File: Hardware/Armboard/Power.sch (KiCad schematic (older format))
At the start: 7 parts

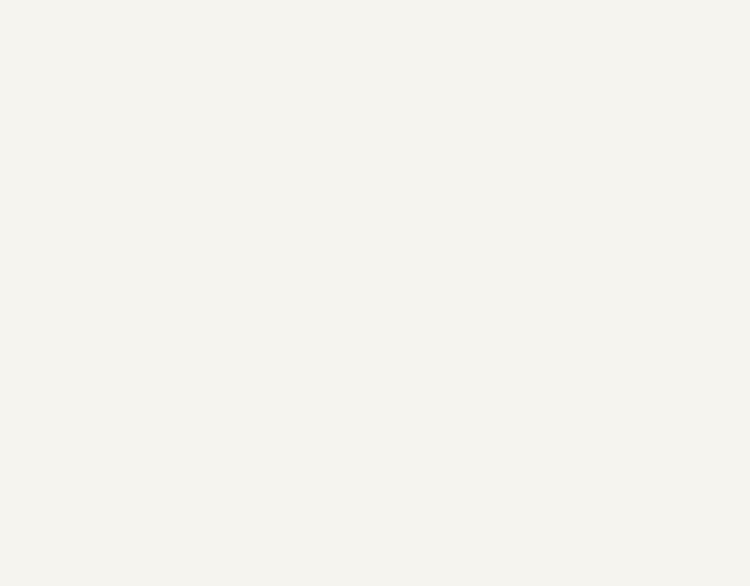
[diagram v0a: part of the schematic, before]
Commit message: Added Anderson connectors to power section
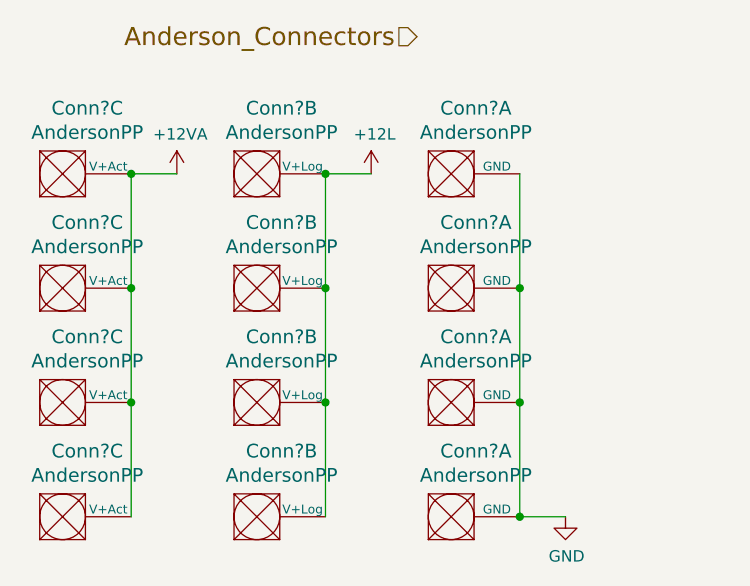
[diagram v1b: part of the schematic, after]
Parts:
- added Conn? (x12): AndersonPP, symbol MRDT_Connectors:AndersonPP
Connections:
- net +12VA: now also Conn?.3 (V+Act), Conn?.3 (V+Act), Conn?.3 (V+Act), Conn?.3 (V+Act)
- net GND: now also Conn?.1 (GND), Conn?.1 (GND), Conn?.1 (GND), Conn?.1 (GND)
- new net +12L: Conn?.2 (V+Log), Conn?.2 (V+Log), Conn?.2 (V+Log), Conn?.2 (V+Log)
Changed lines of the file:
@@
 Text HLabel 9650 1400 0    79   Input ~ 0
 Capacitor_Train
+$Comp
+L MRDT_Connectors:AndersonPP Conn?
+U 3 1 5F67B2AF
+P 2100 2000
+F 0 "Conn?" H 2308 2387 60  0000 C CNN
+F 1 "AndersonPP" H 2308 2281 60  0000 C CNN
+F 2 "" H 1950 1450 60  0001 C CNN
+F 3 "" H 1950 1450 60  0001 C CNN
+	3    2100 2000
+	1    0    0    -1
+$EndComp
+$Comp
+L MRDT_Connectors:AndersonPP Conn?
+U 2 1 5F67B746
+P 2950 2000
+F 0 "Conn?" H 3158 2387 60  0000 C CNN
+F 1 "AndersonPP" H 3158 2281 60  0000 C CNN
+F 2 "" H 2800 1450 60  0001 C CNN
+F 3 "" H 2800 1450 60  0001 C CNN
+	2    2950 2000
+	1    0    0    -1
+$EndComp
+$Comp
+L MRDT_Connectors:AndersonPP Conn?
+U 1 1 5F67BE24
+P 3800 2000
+F 0 "Conn?" H 4008 2387 60  0000 C CNN
+F 1 "AndersonPP" H 4008 2281 60  0000 C CNN
+F 2 "" H 3650 1450 60  0001 C CNN
+F 3 "" H 3650 1450 60  0001 C CNN
+	1    3800 2000
+	1    0    0    -1
+$EndComp
+$Comp
+L MRDT_Connectors:AndersonPP Conn?
+U 3 1 5F67E65A
+P 2100 2500
+F 0 "Conn?" H 2308 2887 60  0000 C CNN
+F 1 "AndersonPP" H 2308 2781 60  0000 C CNN
+F 2 "" H 1950 1950 60  0001 C CNN
+F 3 "" H 1950 1950 60  0001 C CNN
+	3    2100 2500
+	1    0    0    -1
+$EndComp
+$Comp
+L MRDT_Connectors:AndersonPP Conn?
+U 2 1 5F67E660
+P 2950 2500
+F 0 "Conn?" H 3158 2887 60  0000 C CNN
+F 1 "AndersonPP" H 3158 2781 60  0000 C CNN
+F 2 "" H 2800 1950 60  0001 C CNN
+F 3 "" H 2800 1950 60  0001 C CNN
+	2    2950 2500
+	1    0    0    -1
+$EndComp
+$Comp
+L MRDT_Connectors:AndersonPP Conn?
+U 1 1 5F67E666
+P 3800 2500
+F 0 "Conn?" H 4008 2887 60  0000 C CNN
+F 1 "AndersonPP" H 4008 2781 60  0000 C CNN
+F 2 "" H 3650 1950 60  0001 C CNN
+F 3 "" H 3650 1950 60  0001 C CNN
+	1    3800 2500
+	1    0    0    -1
+$EndComp
+$Comp
+L MRDT_Connectors:AndersonPP Conn?
+U 3 1 5F67F13B
+P 2100 3000
+F 0 "Conn?" H 2308 3387 60  0000 C CNN
+F 1 "AndersonPP" H 2308 3281 60  0000 C CNN
+F 2 "" H 1950 2450 60  0001 C CNN
+F 3 "" H 1950 2450 60  0001 C CNN
+	3    2100 3000
+	1    0    0    -1
+$EndComp
+$Comp
+L MRDT_Connectors:AndersonPP Conn?
+U 2 1 5F67F141
+P 2950 3000
+F 0 "Conn?" H 3158 3387 60  0000 C CNN
+F 1 "AndersonPP" H 3158 3281 60  0000 C CNN
+F 2 "" H 2800 2450 60  0001 C CNN
+F 3 "" H 2800 2450 60  0001 C CNN
+	2    2950 3000
+	1    0    0    -1
+$EndComp
+$Comp
+L MRDT_Connectors:AndersonPP Conn?
+U 1 1 5F67F147
+P 3800 3000
+F 0 "Conn?" H 4008 3387 60  0000 C CNN
+F 1 "AndersonPP" H 4008 3281 60  0000 C CNN
+F 2 "" H 3650 2450 60  0001 C CNN
+F 3 "" H 3650 2450 60  0001 C CNN
+	1    3800 3000
+	1    0    0    -1
+$EndComp
+$Comp
+L MRDT_Connectors:AndersonPP Conn?
+U 3 1 5F67F9E7
+P 2100 3500
+F 0 "Conn?" H 2308 3887 60  0000 C CNN
+F 1 "AndersonPP" H 2308 3781 60  0000 C CNN
+F 2 "" H 1950 2950 60  0001 C CNN
+F 3 "" H 1950 2950 60  0001 C CNN
+	3    2100 3500
+	1    0    0    -1
+$EndComp
+$Comp
+L MRDT_Connectors:AndersonPP Conn?
+U 2 1 5F67F9ED
+P 2950 3500
+F 0 "Conn?" H 3158 3887 60  0000 C CNN
+F 1 "AndersonPP" H 3158 3781 60  0000 C CNN
+F 2 "" H 2800 2950 60  0001 C CNN
+F 3 "" H 2800 2950 60  0001 C CNN
+	2    2950 3500
+	1    0    0    -1
+$EndComp
+$Comp
+L MRDT_Connectors:AndersonPP Conn?
+U 1 1 5F67F9F3
+P 3800 3500
+F 0 "Conn?" H 4008 3887 60  0000 C CNN
+F 1 "AndersonPP" H 4008 3781 60  0000 C CNN
+F 2 "" H 3650 2950 60  0001 C CNN
+F 3 "" H 3650 2950 60  0001 C CNN
+	1    3800 3500
+	1    0    0    -1
+$EndComp
+Wire Wire Line
+	2500 3400 2500 2900
+Connection ~ 2500 2400
+Wire Wire Line
+	2500 2400 2500 1900
+Connection ~ 2500 2900
+Wire Wire Line
+	2500 2900 2500 2400
+Wire Wire Line
+	3350 1900 3350 2400
+Connection ~ 3350 2400
+Wire Wire Line
+	3350 2400 3350 2900
+Connection ~ 3350 2900
+Wire Wire Line
+	3350 2900 3350 3400
+Wire Wire Line
+	4200 1900 4200 2400
+Connection ~ 4200 2400
+Wire Wire Line
+	4200 2400 4200 2900
+Connection ~ 4200 2900
+Wire Wire Line
+	4200 2900 4200 3400
+$Comp
+L power:+12VA #PWR?
+U 1 1 5F680A3E
+P 2700 1900
+F 0 "#PWR?" H 2700 1750 50  0001 C CNN
+F 1 "+12VA" H 2715 2073 50  0000 C CNN
+F 2 "" H 2700 1900 50  0001 C CNN
+F 3 "" H 2700 1900 50  0001 C CNN
+	1    2700 1900
+	1    0    0    -1
+$EndComp
+$Comp
+L power:+12L #PWR?
+U 1 1 5F6813B5
+P 3550 1900
+F 0 "#PWR?" H 3550 1750 50  0001 C CNN
+F 1 "+12L" H 3565 2073 50  0000 C CNN
+F 2 "" H 3550 1900 50  0001 C CNN
+F 3 "" H 3550 1900 50  0001 C CNN
+	1    3550 1900
+	1    0    0    -1
+$EndComp
+$Comp
+L power:GND #PWR?
+U 1 1 5F68170C
+P 4400 3400
+F 0 "#PWR?" H 4400 3150 50  0001 C CNN
+F 1 "GND" H 4405 3227 50  0000 C CNN
+F 2 "" H 4400 3400 50  0001 C CNN
+F 3 "" H 4400 3400 50  0001 C CNN
+	1    4400 3400
+	1    0    0    -1
+$EndComp
+Wire Wire Line
+	2500 1900 2700 1900
+Connection ~ 2500 1900
+Wire Wire Line
+	3350 1900 3550 1900
+Connection ~ 3350 1900
+Wire Wire Line
+	4200 3400 4400 3400
+Connection ~ 4200 3400
+Text HLabel 3750 1300 0    79   Input ~ 0
+Anderson_Connectors
 $EndSCHEMATC

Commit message: Power Board Schematic Update
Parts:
- added 10uF: C6, symbol Device:C
- added 10uF: C7, symbol Device:C
- Conn? (x12): symbol MRDT_Connectors:AndersonPP -> Armboard-rescue:AndersonPP-MRDT_Connectors
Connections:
- net +12L: now also 10uF.1
- net GND: now also 10uF.2, 10uF.2
- new net +3V3: 10uF.1
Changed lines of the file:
@@
 Capacitor_Train
 $Comp
-L MRDT_Connectors:AndersonPP Conn?
+L Armboard-rescue:AndersonPP-MRDT_Connectors Conn?
 U 3 1 5F67B2AF
 P 2100 2000
+AR Path="/5F67B2AF" Ref="Conn?"  Part="3"
+AR Path="/5F67ABAC/5F67B2AF" Ref="Conn?"  Part="3"
 F 0 "Conn?" H 2308 2387 60  0000 C CNN
 F 1 "AndersonPP" H 2308 2281 60  0000 C CNN
@@
 $EndComp
 $Comp
-L MRDT_Connectors:AndersonPP Conn?
+L Armboard-rescue:AndersonPP-MRDT_Connectors Conn?
 U 2 1 5F67B746
 P 2950 2000
+AR Path="/5F67B746" Ref="Conn?"  Part="2"
+AR Path="/5F67ABAC/5F67B746" Ref="Conn?"  Part="2"
 F 0 "Conn?" H 3158 2387 60  0000 C CNN
 F 1 "AndersonPP" H 3158 2281 60  0000 C CNN
@@
 $EndComp
 $Comp
-L MRDT_Connectors:AndersonPP Conn?
+L Armboard-rescue:AndersonPP-MRDT_Connectors Conn?
 U 1 1 5F67BE24
 P 3800 2000
+AR Path="/5F67BE24" Ref="Conn?"  Part="1"
+AR Path="/5F67ABAC/5F67BE24" Ref="Conn?"  Part="1"
 F 0 "Conn?" H 4008 2387 60  0000 C CNN
 F 1 "AndersonPP" H 4008 2281 60  0000 C CNN
@@
 $EndComp
 $Comp
-L MRDT_Connectors:AndersonPP Conn?
+L Armboard-rescue:AndersonPP-MRDT_Connectors Conn?
 U 3 1 5F67E65A
 P 2100 2500
+AR Path="/5F67E65A" Ref="Conn?"  Part="3"
+AR Path="/5F67ABAC/5F67E65A" Ref="Conn?"  Part="3"
 F 0 "Conn?" H 2308 2887 60  0000 C CNN
 F 1 "AndersonPP" H 2308 2781 60  0000 C CNN
@@
 $EndComp
 $Comp
-L MRDT_Connectors:AndersonPP Conn?
+L Armboard-rescue:AndersonPP-MRDT_Connectors Conn?
 U 2 1 5F67E660
 P 2950 2500
+AR Path="/5F67E660" Ref="Conn?"  Part="2"
+AR Path="/5F67ABAC/5F67E660" Ref="Conn?"  Part="2"
 F 0 "Conn?" H 3158 2887 60  0000 C CNN
 F 1 "AndersonPP" H 3158 2781 60  0000 C CNN
@@
 $EndComp
 $Comp
-L MRDT_Connectors:AndersonPP Conn?
+L Armboard-rescue:AndersonPP-MRDT_Connectors Conn?
 U 1 1 5F67E666
 P 3800 2500
+AR Path="/5F67E666" Ref="Conn?"  Part="1"
+AR Path="/5F67ABAC/5F67E666" Ref="Conn?"  Part="1"
 F 0 "Conn?" H 4008 2887 60  0000 C CNN
 F 1 "AndersonPP" H 4008 2781 60  0000 C CNN
@@
 $EndComp
 $Comp
-L MRDT_Connectors:AndersonPP Conn?
+L Armboard-rescue:AndersonPP-MRDT_Connectors Conn?
 U 3 1 5F67F13B
 P 2100 3000
+AR Path="/5F67F13B" Ref="Conn?"  Part="3"
+AR Path="/5F67ABAC/5F67F13B" Ref="Conn?"  Part="3"
 F 0 "Conn?" H 2308 3387 60  0000 C CNN
 F 1 "AndersonPP" H 2308 3281 60  0000 C CNN
@@
 $EndComp
 $Comp
-L MRDT_Connectors:AndersonPP Conn?
+L Armboard-rescue:AndersonPP-MRDT_Connectors Conn?
 U 2 1 5F67F141
 P 2950 3000
+AR Path="/5F67F141" Ref="Conn?"  Part="2"
+AR Path="/5F67ABAC/5F67F141" Ref="Conn?"  Part="2"
 F 0 "Conn?" H 3158 3387 60  0000 C CNN
 F 1 "AndersonPP" H 3158 3281 60  0000 C CNN
@@
 $EndComp
 $Comp
-L MRDT_Connectors:AndersonPP Conn?
+L Armboard-rescue:AndersonPP-MRDT_Connectors Conn?
 U 1 1 5F67F147
 P 3800 3000
+AR Path="/5F67F147" Ref="Conn?"  Part="1"
+AR Path="/5F67ABAC/5F67F147" Ref="Conn?"  Part="1"
 F 0 "Conn?" H 4008 3387 60  0000 C CNN
 F 1 "AndersonPP" H 4008 3281 60  0000 C CNN
@@
 $EndComp
 $Comp
-L MRDT_Connectors:AndersonPP Conn?
+L Armboard-rescue:AndersonPP-MRDT_Connectors Conn?
 U 3 1 5F67F9E7
 P 2100 3500
+AR Path="/5F67F9E7" Ref="Conn?"  Part="3"
+AR Path="/5F67ABAC/5F67F9E7" Ref="Conn?"  Part="3"
 F 0 "Conn?" H 2308 3887 60  0000 C CNN
 F 1 "AndersonPP" H 2308 3781 60  0000 C CNN
@@
 $EndComp
 $Comp
-L MRDT_Connectors:AndersonPP Conn?
+L Armboard-rescue:AndersonPP-MRDT_Connectors Conn?
 U 2 1 5F67F9ED
 P 2950 3500
+AR Path="/5F67F9ED" Ref="Conn?"  Part="2"
+AR Path="/5F67ABAC/5F67F9ED" Ref="Conn?"  Part="2"
 F 0 "Conn?" H 3158 3887 60  0000 C CNN
 F 1 "AndersonPP" H 3158 3781 60  0000 C CNN
@@
 $EndComp
 $Comp
-L MRDT_Connectors:AndersonPP Conn?
+L Armboard-rescue:AndersonPP-MRDT_Connectors Conn?
 U 1 1 5F67F9F3
 P 3800 3500
+AR Path="/5F67F9F3" Ref="Conn?"  Part="1"
+AR Path="/5F67ABAC/5F67F9F3" Ref="Conn?"  Part="1"
 F 0 "Conn?" H 4008 3887 60  0000 C CNN
 F 1 "AndersonPP" H 4008 3781 60  0000 C CNN
@@
 Text HLabel 3750 1300 0    79   Input ~ 0
 Anderson_Connectors
+$Comp
+L power:+12L #PWR?
+U 1 1 5F67B836
+P 8500 2750
+F 0 "#PWR?" H 8500 2600 50  0001 C CNN
+F 1 "+12L" H 8515 2923 50  0000 C CNN
+F 2 "" H 8500 2750 50  0001 C CNN
+F 3 "" H 8500 2750 50  0001 C CNN
+	1    8500 2750
+	1    0    0    -1
+$EndComp
+$Comp
+L power:+3.3V #PWR?
+U 1 1 5F67BC4F
+P 10000 2700
+F 0 "#PWR?" H 10000 2550 50  0001 C CNN
+F 1 "+3.3V" H 10015 2873 50  0000 C CNN
+F 2 "" H 10000 2700 50  0001 C CNN
+F 3 "" H 10000 2700 50  0001 C CNN
+	1    10000 2700
+	1    0    0    -1
+$EndComp
+$Comp
+L Device:C 10uF
+U 1 1 5F67C9C2
+P 8500 3200
+F 0 "10uF" H 8615 3246 50  0000 L CNN
+F 1 "C6" H 8615 3155 50  0000 L CNN
+F 2 "" H 8538 3050 50  0001 C CNN
+F 3 "~" H 8500 3200 50  0001 C CNN
+	1    8500 3200
+	1    0    0    -1
+$EndComp
+$Comp
+L Device:C 10uF
+U 1 1 5F67D17F
+P 10000 3200
+F 0 "10uF" H 10115 3246 50  0000 L CNN
+F 1 "C7" H 10115 3155 50  0000 L CNN
+F 2 "" H 10038 3050 50  0001 C CNN
+F 3 "~" H 10000 3200 50  0001 C CNN
+	1    10000 3200
+	1    0    0    -1
+$EndComp
+Wire Wire Line
+	8500 2750 8500 3050
+Wire Wire Line
+	8500 3350 10000 3350
+Wire Wire Line
+	10000 3350 10250 3350
+Wire Wire Line
+	10250 3350 10250 3500
+Connection ~ 10000 3350
+Wire Wire Line
+	10000 2700 10000 3050
+$Comp
+L power:GND #PWR?
+U 1 1 5F6806AC
+P 10250 3500
+F 0 "#PWR?" H 10250 3250 50  0001 C CNN
+F 1 "GND" H 10255 3327 50  0000 C CNN
+F 2 "" H 10250 3500 50  0001 C CNN
+F 3 "" H 10250 3500 50  0001 C CNN
+	1    10250 3500
+	1    0    0    -1
+$EndComp
 $EndSCHEMATC

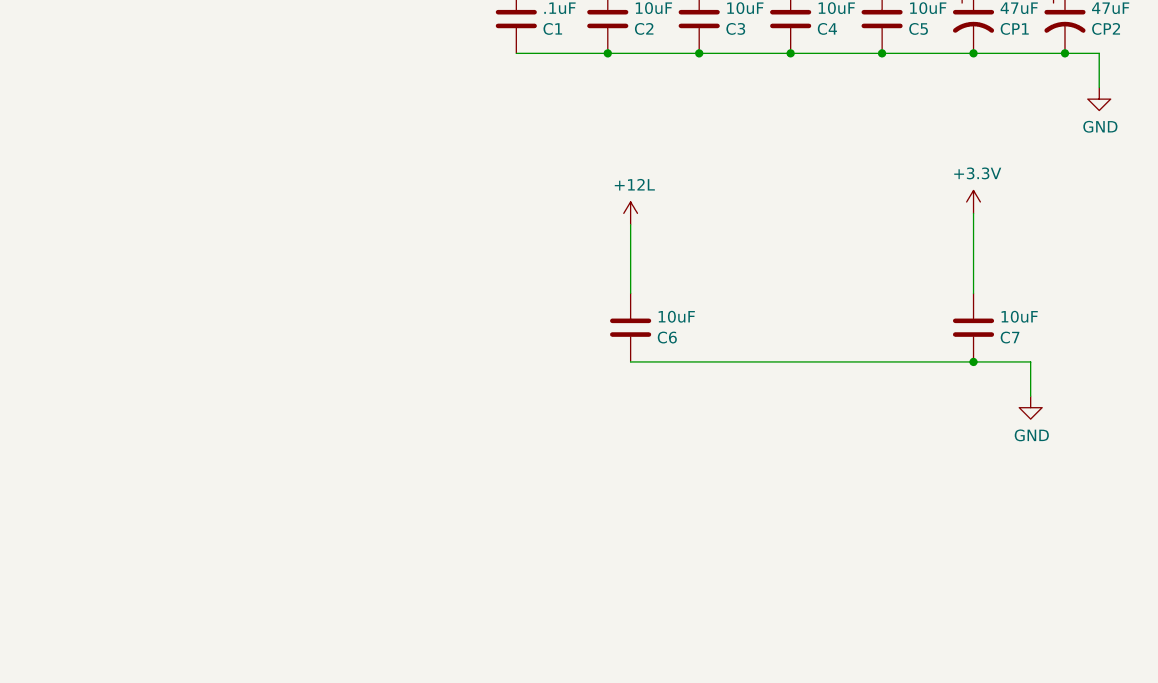
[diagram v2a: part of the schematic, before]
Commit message: Added OKI to power
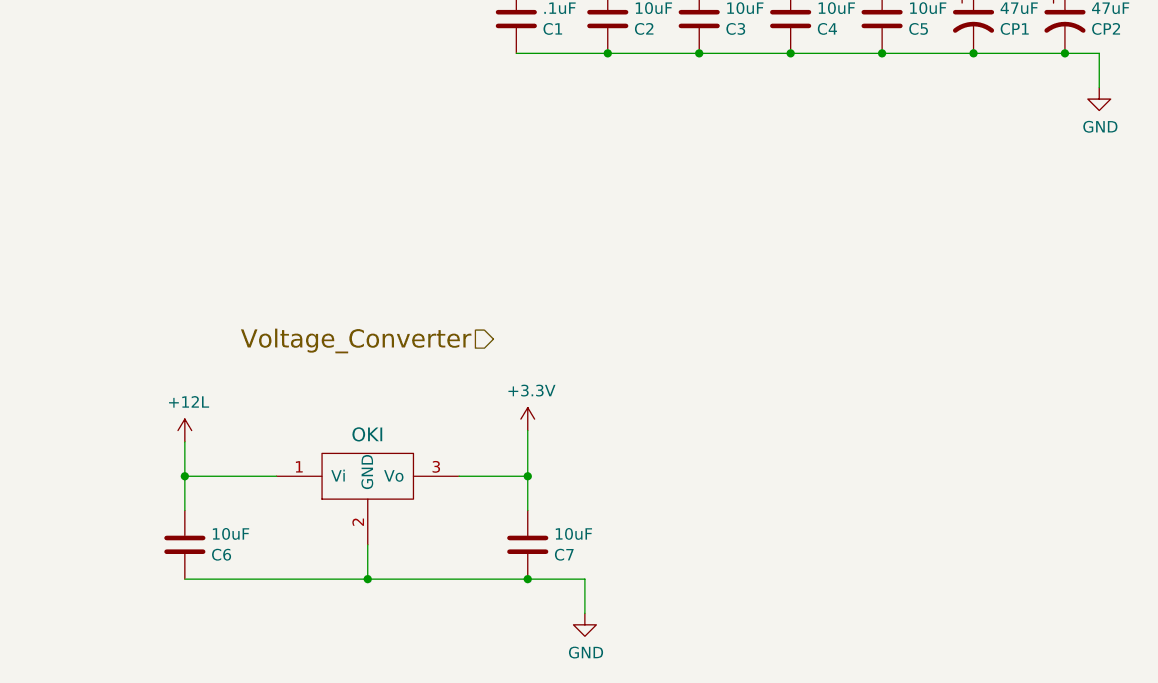
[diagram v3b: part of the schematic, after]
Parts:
- added U?: OKI, symbol MRDT_Devices:OKI
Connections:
- net +12L: now also U?.1 (Vi)
- net +3V3: now also U?.3 (Vo)
- net GND: now also U?.2 (GND)
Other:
- moved on the sheet: 10uF
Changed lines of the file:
@@
 L power:+12L #PWR?
 U 1 1 5F67B836
-P 8500 2750
-F 0 "#PWR?" H 8500 2600 50  0001 C CNN
-F 1 "+12L" H 8515 2923 50  0000 C CNN
-F 2 "" H 8500 2750 50  0001 C CNN
-F 3 "" H 8500 2750 50  0001 C CNN
-	1    8500 2750
+P 6550 3700
+F 0 "#PWR?" H 6550 3550 50  0001 C CNN
+F 1 "+12L" H 6565 3873 50  0000 C CNN
+F 2 "" H 6550 3700 50  0001 C CNN
+F 3 "" H 6550 3700 50  0001 C CNN
+	1    6550 3700
 	1    0    0    -1
 $EndComp
@@
 L power:+3.3V #PWR?
 U 1 1 5F67BC4F
-P 10000 2700
-F 0 "#PWR?" H 10000 2550 50  0001 C CNN
-F 1 "+3.3V" H 10015 2873 50  0000 C CNN
-F 2 "" H 10000 2700 50  0001 C CNN
-F 3 "" H 10000 2700 50  0001 C CNN
-	1    10000 2700
+P 8050 3650
+F 0 "#PWR?" H 8050 3500 50  0001 C CNN
+F 1 "+3.3V" H 8065 3823 50  0000 C CNN
+F 2 "" H 8050 3650 50  0001 C CNN
+F 3 "" H 8050 3650 50  0001 C CNN
+	1    8050 3650
 	1    0    0    -1
 $EndComp
@@
 L Device:C 10uF
 U 1 1 5F67C9C2
-P 8500 3200
-F 0 "10uF" H 8615 3246 50  0000 L CNN
-F 1 "C6" H 8615 3155 50  0000 L CNN
-F 2 "" H 8538 3050 50  0001 C CNN
-F 3 "~" H 8500 3200 50  0001 C CNN
-	1    8500 3200
+P 6550 4150
+F 0 "10uF" H 6665 4196 50  0000 L CNN
+F 1 "C6" H 6665 4105 50  0000 L CNN
+F 2 "" H 6588 4000 50  0001 C CNN
+F 3 "~" H 6550 4150 50  0001 C CNN
+	1    6550 4150
 	1    0    0    -1
 $EndComp
@@
 L Device:C 10uF
 U 1 1 5F67D17F
-P 10000 3200
-F 0 "10uF" H 10115 3246 50  0000 L CNN
-F 1 "C7" H 10115 3155 50  0000 L CNN
-F 2 "" H 10038 3050 50  0001 C CNN
-F 3 "~" H 10000 3200 50  0001 C CNN
-	1    10000 3200
+P 8050 4150
+F 0 "10uF" H 8165 4196 50  0000 L CNN
+F 1 "C7" H 8165 4105 50  0000 L CNN
+F 2 "" H 8088 4000 50  0001 C CNN
+F 3 "~" H 8050 4150 50  0001 C CNN
+	1    8050 4150
 	1    0    0    -1
 $EndComp
 Wire Wire Line
-	8500 2750 8500 3050
+	6550 3700 6550 3850
 Wire Wire Line
-	8500 3350 10000 3350
+	6550 4300 7350 4300
 Wire Wire Line
-	10000 3350 10250 3350
+	8050 4300 8300 4300
 Wire Wire Line
-	10250 3350 10250 3500
-Connection ~ 10000 3350
+	8300 4300 8300 4450
+Connection ~ 8050 4300
 Wire Wire Line
-	10000 2700 10000 3050
+	8050 3650 8050 3850
 $Comp
 L power:GND #PWR?
 U 1 1 5F6806AC
-P 10250 3500
-F 0 "#PWR?" H 10250 3250 50  0001 C CNN
-F 1 "GND" H 10255 3327 50  0000 C CNN
-F 2 "" H 10250 3500 50  0001 C CNN
-F 3 "" H 10250 3500 50  0001 C CNN
-	1    10250 3500
+P 8300 4450
+F 0 "#PWR?" H 8300 4200 50  0001 C CNN
+F 1 "GND" H 8305 4277 50  0000 C CNN
+F 2 "" H 8300 4450 50  0001 C CNN
+F 3 "" H 8300 4450 50  0001 C CNN
+	1    8300 4450
 	1    0    0    -1
 $EndComp
+$Comp
+L MRDT_Devices:OKI U?
+U 1 1 5F67BA9E
+P 7150 3950
+F 0 "U?" H 7200 3900 60  0001 C CNN
+F 1 "OKI" H 7350 4231 60  0000 C CNN
+F 2 "" H 6950 3850 60  0001 C CNN
+F 3 "" H 6950 3850 60  0001 C CNN
+	1    7150 3950
+	1    0    0    -1
+$EndComp
+Wire Wire Line
+	6950 3850 6550 3850
+Connection ~ 6550 3850
+Wire Wire Line
+	6550 3850 6550 4000
+Wire Wire Line
+	7350 4150 7350 4300
+Connection ~ 7350 4300
+Wire Wire Line
+	7350 4300 8050 4300
+Wire Wire Line
+	7750 3850 8050 3850
+Connection ~ 8050 3850
+Wire Wire Line
+	8050 3850 8050 4000
+Text HLabel 7900 3250 0    79   Input ~ 0
+Voltage_Converter
 $EndSCHEMATC
